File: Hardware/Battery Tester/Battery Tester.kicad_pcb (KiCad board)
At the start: 2 copper layers, 20 x 30 mm, 17 parts, among them J1 USB4105-GF-A, SW1 SW_SPST, U1 MCP73831-5-OT, U2 LP5907MFX-3.3_NOPB

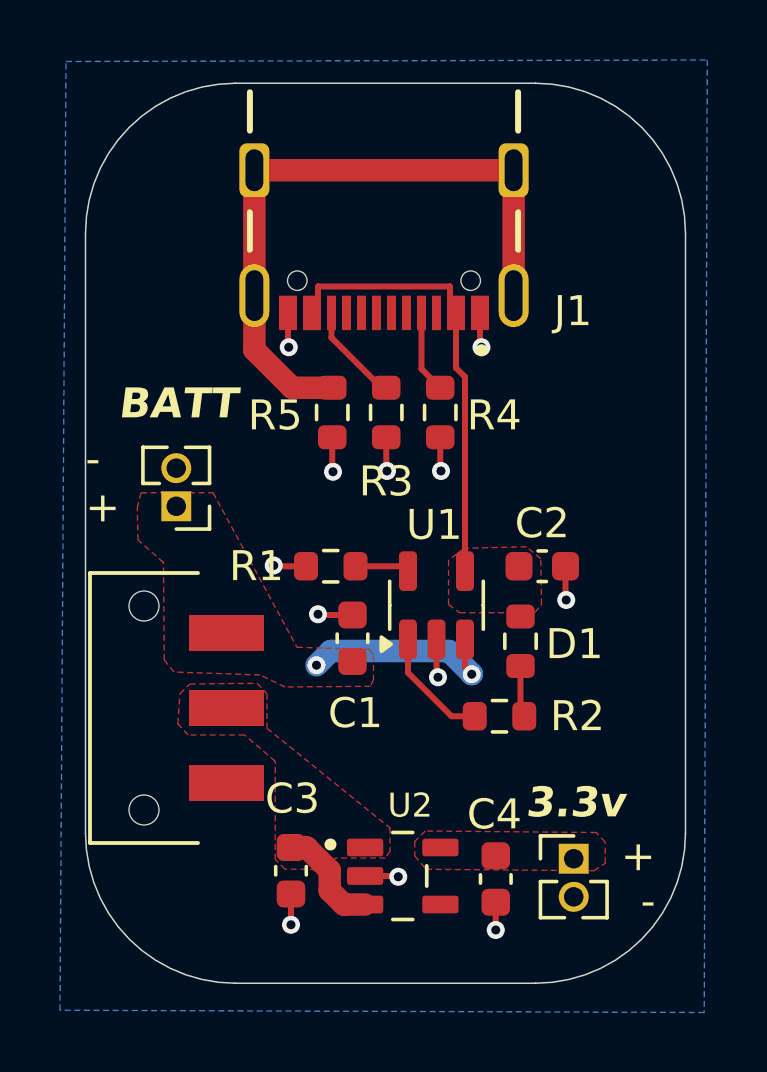
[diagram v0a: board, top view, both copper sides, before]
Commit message: Adding PDFs for the schematics
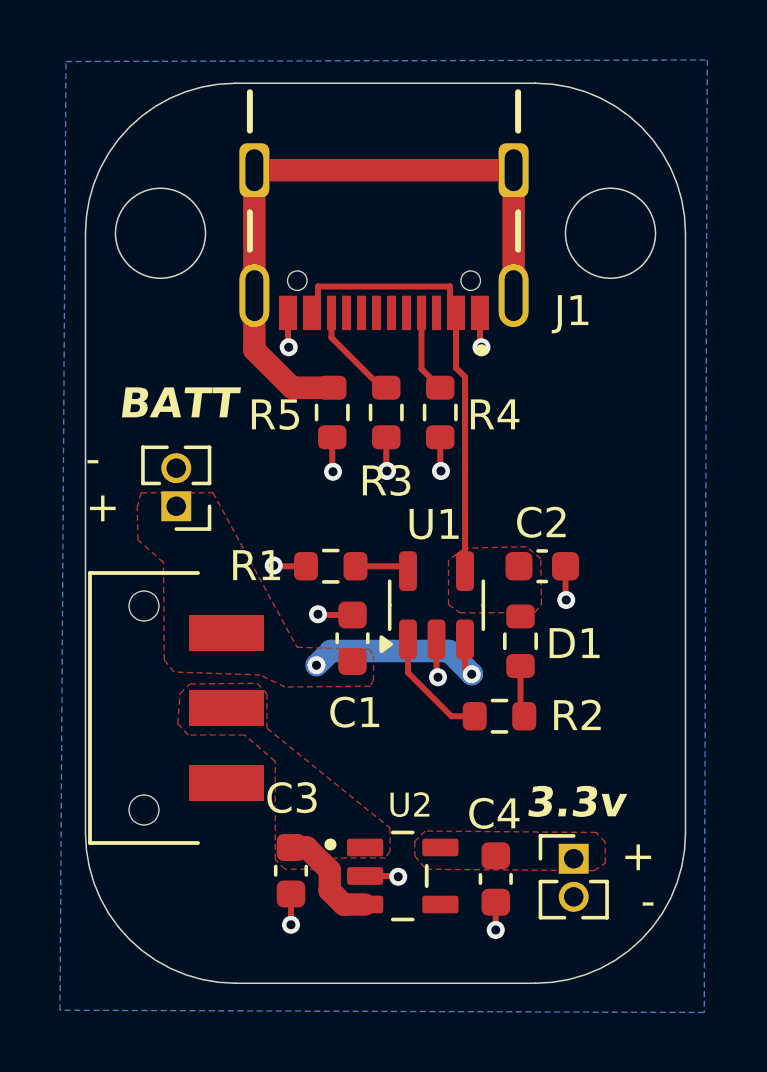
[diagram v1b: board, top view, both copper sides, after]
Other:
- outline, holes or cut-outs redrawn
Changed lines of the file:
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@@
 		)
+	)
+	(gr_circle
+		(center 157.5 95)
+		(end 157.5 96.5)
+		(stroke
+			(width 0.05)
+			(type default)
+		)
+		(fill none)
+		(layer "Edge.Cuts")
 	)
 	(gr_line
@@
 			(type default)
 		)
+		(layer "Edge.Cuts")
+	)
+	(gr_circle
+		(center 142.5 95)
+		(end 142.5 96.5)
+		(stroke
+			(width 0.05)
+			(type default)
+		)
+		(fill none)
 		(layer "Edge.Cuts")
 	)
@@
 		)
 	)
+	(dimension
+		(type aligned)
+		(layer "Edge.Cuts")
+		(pts
+			(xy 140 80) (xy 160 80)
+		)
+		(height 0)
+		(gr_text "20.0000 mm"
+			(at 150 78.85 0)
+			(layer "Edge.Cuts")
+			(effects
+				(font
+					(size 1 1)
+					(thickness 0.15)
+				)
+			)
+		)
+		(format
+			(prefix "")
+			(suffix "")
+			(units 3)
+			(units_format 1)
+			(precision 4)
+		)
+		(style
+			(thickness 0.05)
+			(arrow_length 1.27)
+			(text_position_mode 0)
+			(extension_height 0.58642)
+			(extension_offset 0.5) keep_text_aligned)
+	)
+	(dimension
+		(type aligned)
+		(layer "Edge.Cuts")
+		(pts
+			(xy 165 90) (xy 165 120)
+		)
+		(height -5)
+		(gr_text "30.0000 mm"
+			(at 168.85 105 90)
+			(layer "Edge.Cuts")
+			(effects
+				(font
+					(size 1 1)
+					(thickness 0.15)
+				)
+			)
+		)
+		(format
+			(prefix "")
+			(suffix "")
+			(units 3)
+			(units_format 1)
+			(precision 4)
+		)
+		(style
+			(thickness 0.05)
+			(arrow_length 1.27)
+			(text_position_mode 0)
+			(extension_height 0.58642)
+			(extension_offset 0.5) keep_text_aligned)
+	)
 	(segment
